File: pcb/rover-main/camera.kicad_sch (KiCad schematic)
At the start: 0 parts

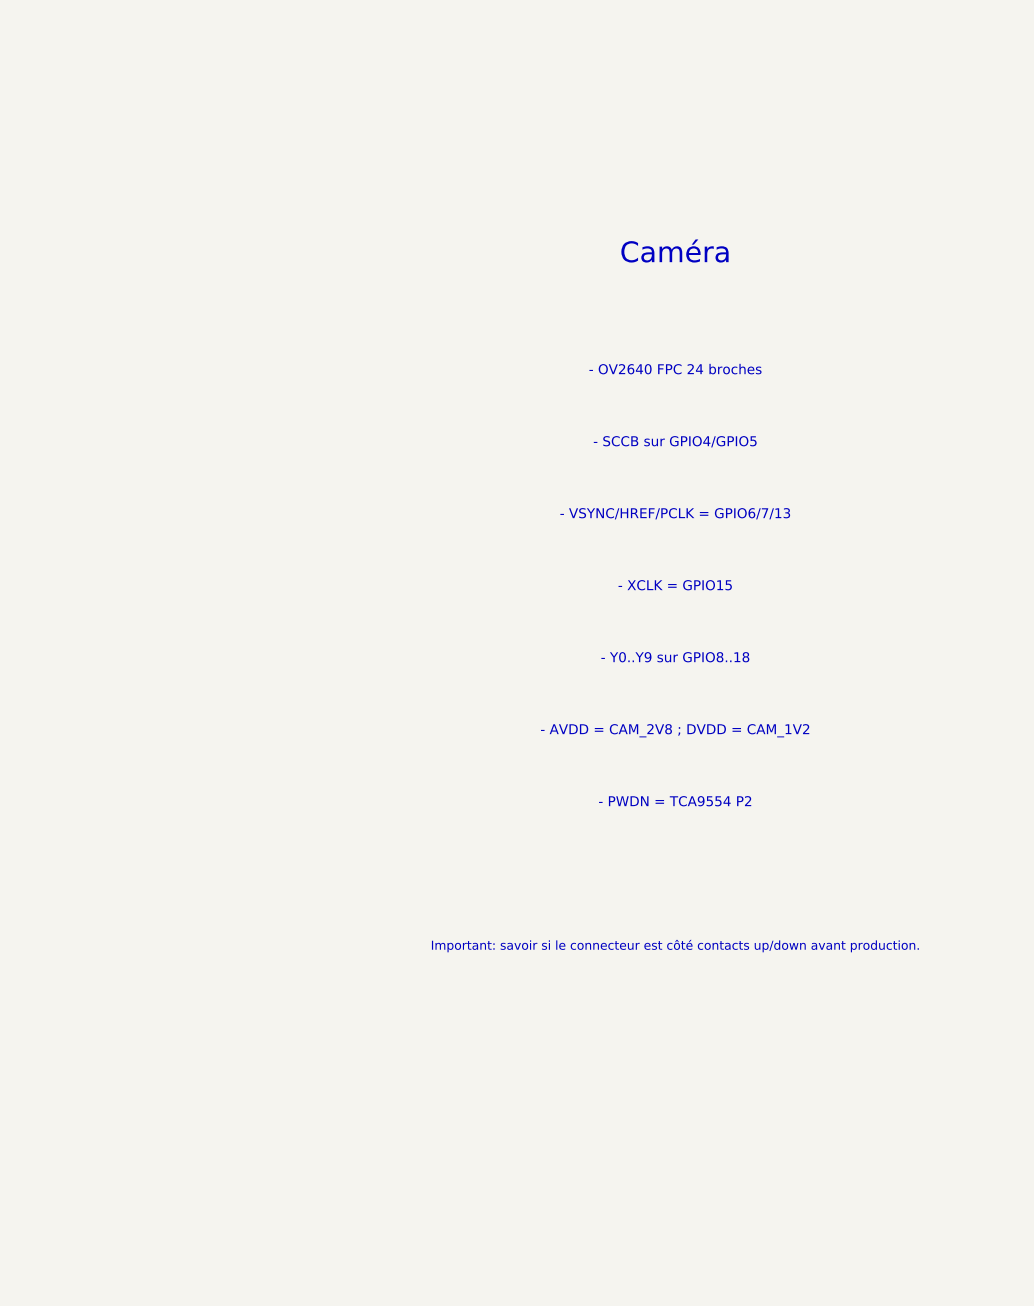
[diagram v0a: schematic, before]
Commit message: Add a more concrete KiCad schematic draft with key blocks and real net names for the Rover PCB design.
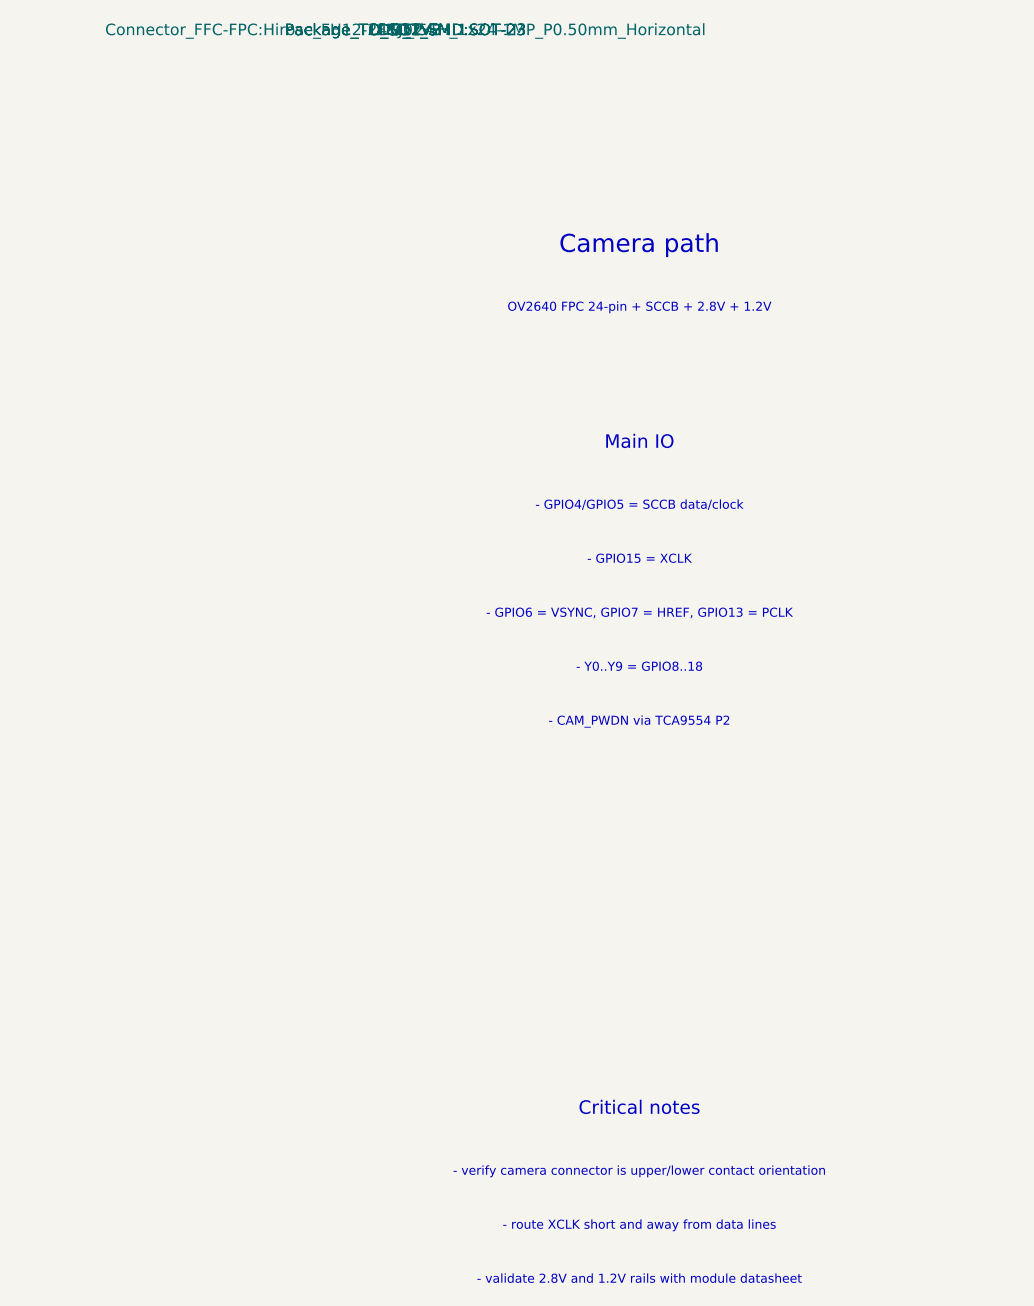
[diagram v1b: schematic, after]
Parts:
- added J5: FPC_24, Connector_FFC-FPC:Hirose_FH12-24S-0.5SH_1x24-1MP_P0.50mm_Horizontal, symbol Connector:Conn_01x24_Female
- added U11: LDO_2V8, Package_TO_SOT_SMD:SOT-23, symbol Regulator_Linear:XC6206P282
- added U12: LDO_1V2, Package_TO_SOT_SMD:SOT-23, symbol Regulator_Linear:XC6206P122
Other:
- note added: "- CAM_PWDN via TCA9554 P2"
- note added: "- GPIO15 = XCLK"
- note added: "- GPIO4/GPIO5 = SCCB data/clock"
- note added: "- GPIO6 = VSYNC, GPIO7 = HREF, GPIO13 = PCLK"
- note added: "- Y0..Y9 = GPIO8..18"
- note added: "- route XCLK short and away from data lines"
- note added: "- validate 2.8V and 1.2V rails with module datasheet"
- note added: "- verify camera connector is upper/lower contact orientation"
- note added: "Camera path"
- note added: "Critical notes"
- note added: "Main IO"
- note added: "OV2640 FPC 24-pin + SCCB + 2.8V + 1.2V"
- note removed: "- AVDD = CAM_2V8 ; DVDD = CAM_1V2"
- note removed: "- OV2640 FPC 24 broches"
- note removed: "- PWDN = TCA9554 P2"
- note removed: "- SCCB sur GPIO4/GPIO5"
- note removed: "- VSYNC/HREF/PCLK = GPIO6/7/13"
- note removed: "- XCLK = GPIO15"
- note removed: "- Y0..Y9 sur GPIO8..18"
- note removed: "Caméra"
- note removed: "Important: savoir si le connecteur est côté contacts up/down avant production."
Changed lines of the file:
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@@
 (kicad_sch
-  (version 20250114)
-  (generator "KiCad")
+  (version 20211014)
+  (generator "eeschema")
   (paper "A4")
   (title_block
     (title "Rover PCB - camera")
     (date "2026-10-13")
-    (rev "0.1")
+    (rev "0.2")
     (company "Rover Project")
-    (comment 1 "Draft only - confirm camera pin map")
+    (comment 1 "Draft schematic - verify OV2640 FPC pinout and orientation")
   )
-  (text "Caméra" (at 30 25 0)
-    (effects (font (size 2.3 2.3) (thickness 0.3)))
+  (text "Camera path" (at 26 24 0)
+    (effects (font (size 2.0 2.0) (thickness 0.2)))
   )
-  (text "- OV2640 FPC 24 broches" (at 30 38 0)
-    (effects (font (size 1.1 1.1)))
-  )
-  (text "- SCCB sur GPIO4/GPIO5" (at 30 46 0)
-    (effects (font (size 1.1 1.1)))
-  )
-  (text "- VSYNC/HREF/PCLK = GPIO6/7/13" (at 30 54 0)
-    (effects (font (size 1.1 1.1)))
-  )
-  (text "- XCLK = GPIO15" (at 30 62 0)
-    (effects (font (size 1.1 1.1)))
-  )
-  (text "- Y0..Y9 sur GPIO8..18" (at 30 70 0)
-    (effects (font (size 1.1 1.1)))
-  )
-  (text "- AVDD = CAM_2V8 ; DVDD = CAM_1V2" (at 30 78 0)
-    (effects (font (size 1.1 1.1)))
-  )
-  (text "- PWDN = TCA9554 P2" (at 30 86 0)
-    (effects (font (size 1.1 1.1)))
-  )
-  (text "Important: savoir si le connecteur est côté contacts up/down avant production." (at 30 102 0)
+  (text "OV2640 FPC 24-pin + SCCB + 2.8V + 1.2V" (at 26 31 0)
     (effects (font (size 1.0 1.0)))
   )
+  (text "Main IO" (at 26 46 0)
+    (effects (font (size 1.5 1.5) (thickness 0.2)))
+  )
+  (text "- GPIO4/GPIO5 = SCCB data/clock" (at 26 53 0)
+    (effects (font (size 1.0 1.0)))
+  )
+  (text "- GPIO15 = XCLK" (at 26 59 0)
+    (effects (font (size 1.0 1.0)))
+  )
+  (text "- GPIO6 = VSYNC, GPIO7 = HREF, GPIO13 = PCLK" (at 26 65 0)
+    (effects (font (size 1.0 1.0)))
+  )
+  (text "- Y0..Y9 = GPIO8..18" (at 26 71 0)
+    (effects (font (size 1.0 1.0)))
+  )
+  (text "- CAM_PWDN via TCA9554 P2" (at 26 77 0)
+    (effects (font (size 1.0 1.0)))
+  )
+  (symbol
+    (lib_id "Connector:Conn_01x24_Female")
+    (at 150 110 0)
+    (unit 1)
+    (in_bom yes)
+    (property "Reference" "J5")
+    (property "Value" "FPC_24")
+    (property "Footprint" "Connector_FFC-FPC:Hirose_FH12-24S-0.5SH_1x24-1MP_P0.50mm_Horizontal")
+  )
+  (symbol
+    (lib_id "Regulator_Linear:XC6206P282")
+    (at 260 110 0)
+    (unit 1)
+    (in_bom yes)
+    (property "Reference" "U11")
+    (property "Value" "LDO_2V8")
+    (property "Footprint" "Package_TO_SOT_SMD:SOT-23")
+  )
+  (symbol
+    (lib_id "Regulator_Linear:XC6206P122")
+    (at 330 110 0)
+    (unit 1)
+    (in_bom yes)
+    (property "Reference" "U12")
+    (property "Value" "LDO_1V2")
+    (property "Footprint" "Package_TO_SOT_SMD:SOT-23")
+  )
+  (text "Critical notes" (at 26 120 0)
+    (effects (font (size 1.5 1.5) (thickness 0.2)))
+  )
+  (text "- verify camera connector is upper/lower contact orientation" (at 26 127 0)
+    (effects (font (size 1.0 1.0)))
+  )
+  (text "- route XCLK short and away from data lines" (at 26 133 0)
+    (effects (font (size 1.0 1.0)))
+  )
+  (text "- validate 2.8V and 1.2V rails with module datasheet" (at 26 139 0)
+    (effects (font (size 1.0 1.0)))
+  )
